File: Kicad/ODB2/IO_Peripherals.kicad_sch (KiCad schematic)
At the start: 15 parts, among them J1 USB_B_Micro, U4 USBLC6-2P6

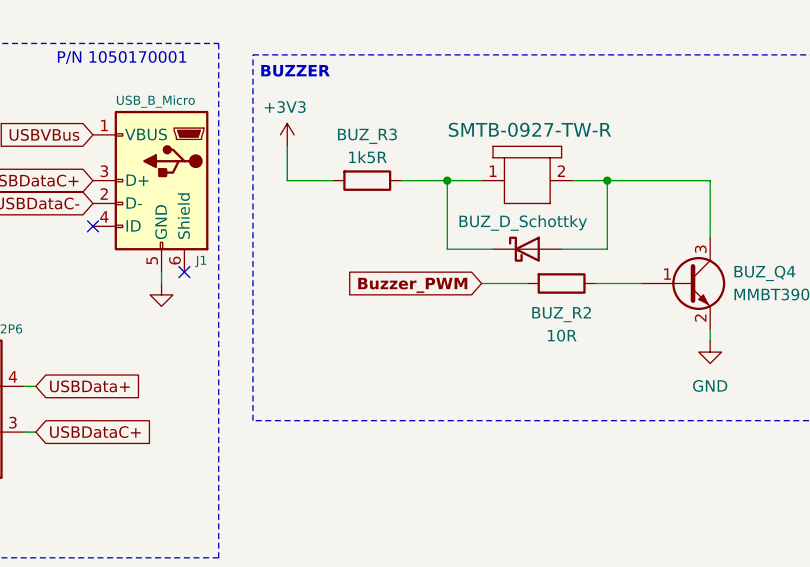
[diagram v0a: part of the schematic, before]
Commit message: merge all sensors to main page + fix NC
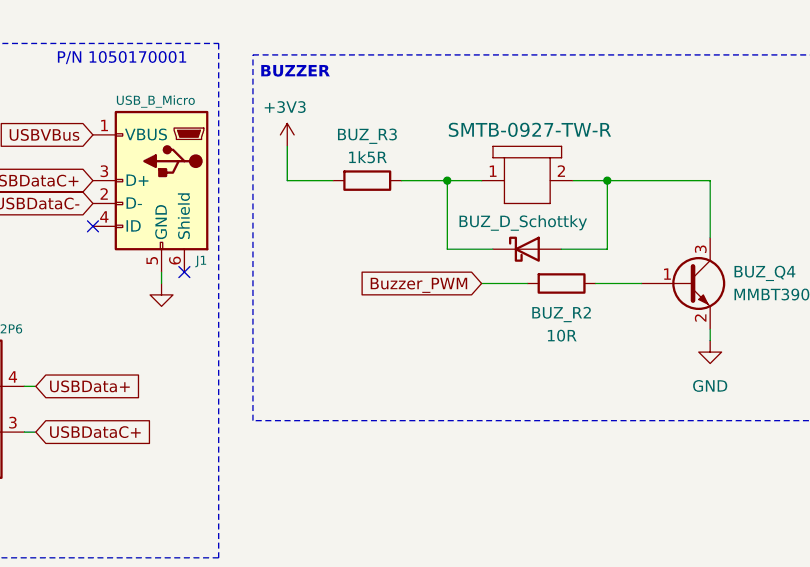
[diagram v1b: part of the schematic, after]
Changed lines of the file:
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@@
 			(font
 				(size 1.27 1.27)
-				(thickness 0.254)
-				(bold yes)
+				(thickness 0.1588)
 			)
 			(justify right)
 		)
 		(property "Intersheetrefs" "${INTERSHEET_REFS}"
-			(at 119.6684 48.26 0)
+			(at 120.1444 48.26 0)
 			(effects
 				(font

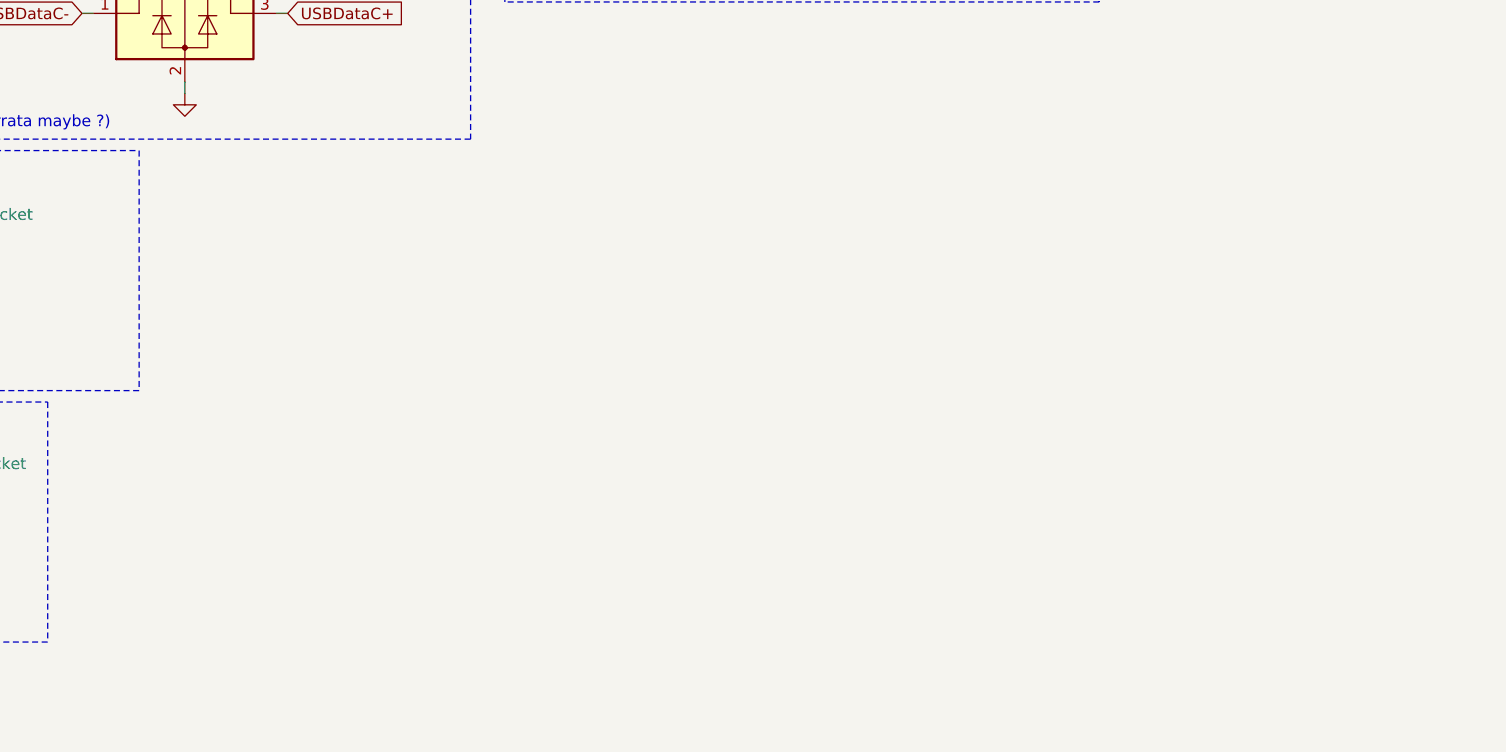
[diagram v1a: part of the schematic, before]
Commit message: delete hierarchie ODB
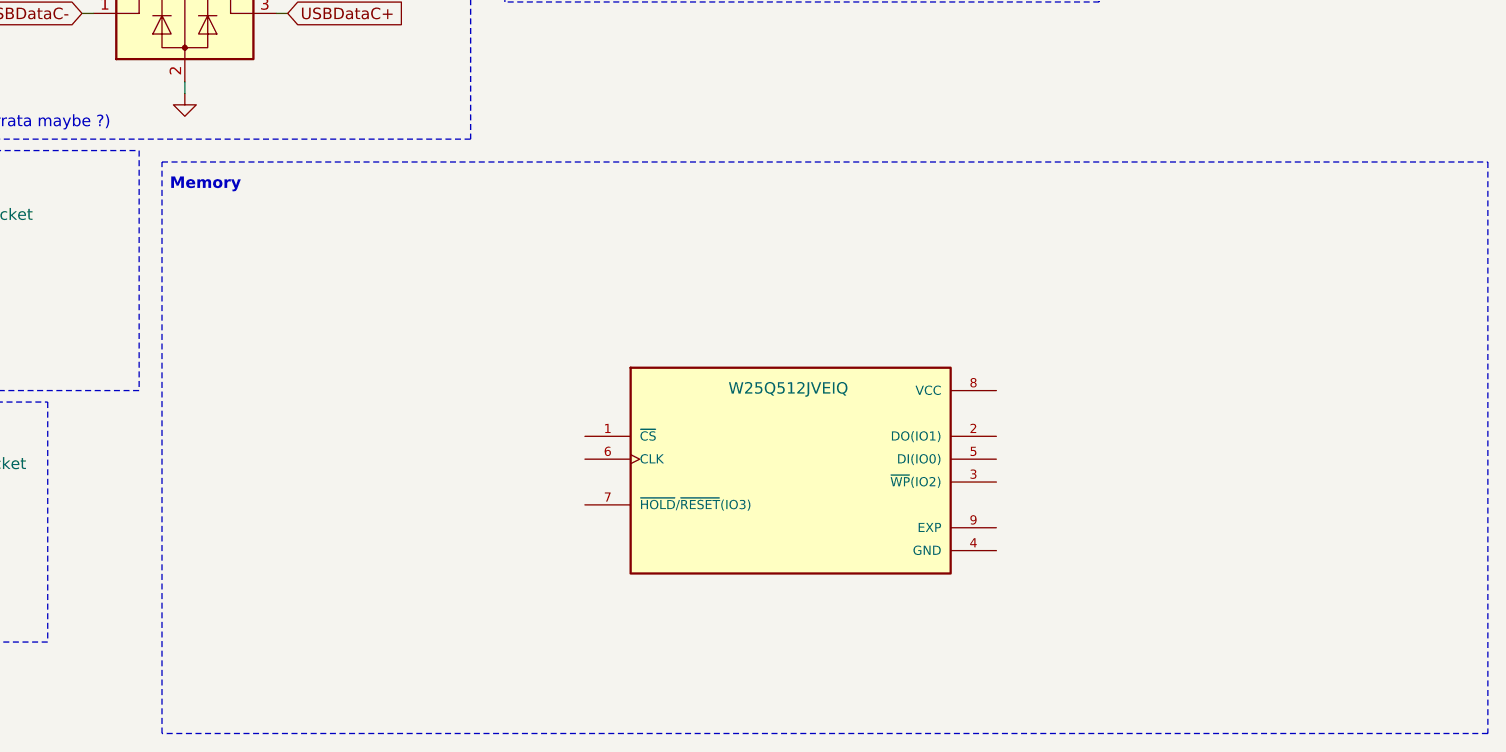
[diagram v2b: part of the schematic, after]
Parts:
- added U10: W25Q512JVEIQ, W25Q512JVEIQ:SON127P600X800X80-9N, symbol ODB_Lib:W25Q512JVEIQ
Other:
- note added: "Memory"
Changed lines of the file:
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@@
+	)
+	(rectangle
+		(start 71.12 81.28)
+		(end 218.44 144.78)
+		(stroke
+			(width 0)
+			(type dash)
+		)
+		(fill
+			(type none)
+		)
 	)
 	(rectangle
@@
 		)
 	)
+	(text "Memory"
+		(exclude_from_sim no)
+		(at 75.946 83.82 0)
+		(effects
+			(font
+				(size 1.27 1.27)
+				(thickness 0.254)
+				(bold yes)
+			)
+		)
+	)
 	(text "MICRO USB"
 		(exclude_from_sim no)
@@
 					(unit 1)
 				)
+			)
+		)
+	)
+	(symbol
+		(lib_id "ODB_Lib:W25Q512JVEIQ")
+		(at 140.97 116.84 0)
+		(unit 1)
+		(exclude_from_sim no)
+		(in_bom yes)
+		(on_board yes)
+		(dnp no)
+		(property "Reference" "U10"
+			(at 140.97 99.06 0)
+			(effects
+				(font
+					(size 1.27 1.27)
+				)
+				(hide yes)
+			)
+		)
+		(property "Value" "W25Q512JVEIQ"
+			(at 140.716 106.426 0)
+			(effects
+				(font
+					(size 1.27 1.27)
+				)
+			)
+		)
+		(property "Footprint" "W25Q512JVEIQ:SON127P600X800X80-9N"
+			(at 151.384 137.922 0)
+			(effects
+				(font
+					(size 1.27 1.27)
+				)
+				(justify bottom)
+				(hide yes)
+			)
+		)
+		(property "Datasheet" ""
+			(at 140.97 116.84 0)
+			(effects
+				(font
+					(size 1.27 1.27)
+				)
+				(hide yes)
+			)
+		)
+		(property "Description" ""
+			(at 140.97 116.84 0)
+			(effects
+				(font
+					(size 1.27 1.27)
+				)
+				(hide yes)
+			)
+		)
+		(property "PARTREV" "G"
+			(at 137.414 131.572 0)
+			(effects
+				(font
+					(size 1.27 1.27)
+				)
+				(justify bottom)
+				(hide yes)
+			)
+		)
+		(property "SNAPEDA_PN" "W25Q512JVEIQ"
+			(at 147.32 131.318 0)
+			(effects
+				(font
+					(size 1.27 1.27)
+				)
+				(justify bottom)
+				(hide yes)
+			)
+		)
+		(property "MANUFACTURER" "Winbond Electronics"
+			(at 148.59 133.096 0)
+			(effects
+				(font
+					(size 1.27 1.27)
+				)
+				(justify bottom)
+				(hide yes)
+			)
+		)
+		(property "MAXIMUM_PACKAGE_HEIGHT" "0.8 mm"
+			(at 137.668 134.874 0)
+			(effects
+				(font
+					(size 1.27 1.27)
+				)
+				(justify bottom)
+				(hide yes)
+			)
+		)
+		(property "STANDARD" "IPC 7351B"
+			(at 147.574 135.128 0)
+			(effects
+				(font
+					(size 1.27 1.27)
+				)
+				(justify bottom)
+				(hide yes)
+			)
+		)
+		(pin "9"
+		)
+		(pin "1"
+		)
+		(pin "5"
+		)
+		(pin "6"
+		)
+		(pin "8"
+		)
+		(pin "4"
+		)
+		(pin "3"
+		)
+		(pin "7"
+		)
+		(pin "2"
+		)
+		(instances
+			(project ""
+				(path "/4b06c5d1-aa8b-48ed-8972-b43a60cfab78/93865dc8-71fa-4dc6-90ce-f5a9779dfd41"
+					(reference "U10")
+					(unit 1)
+				)

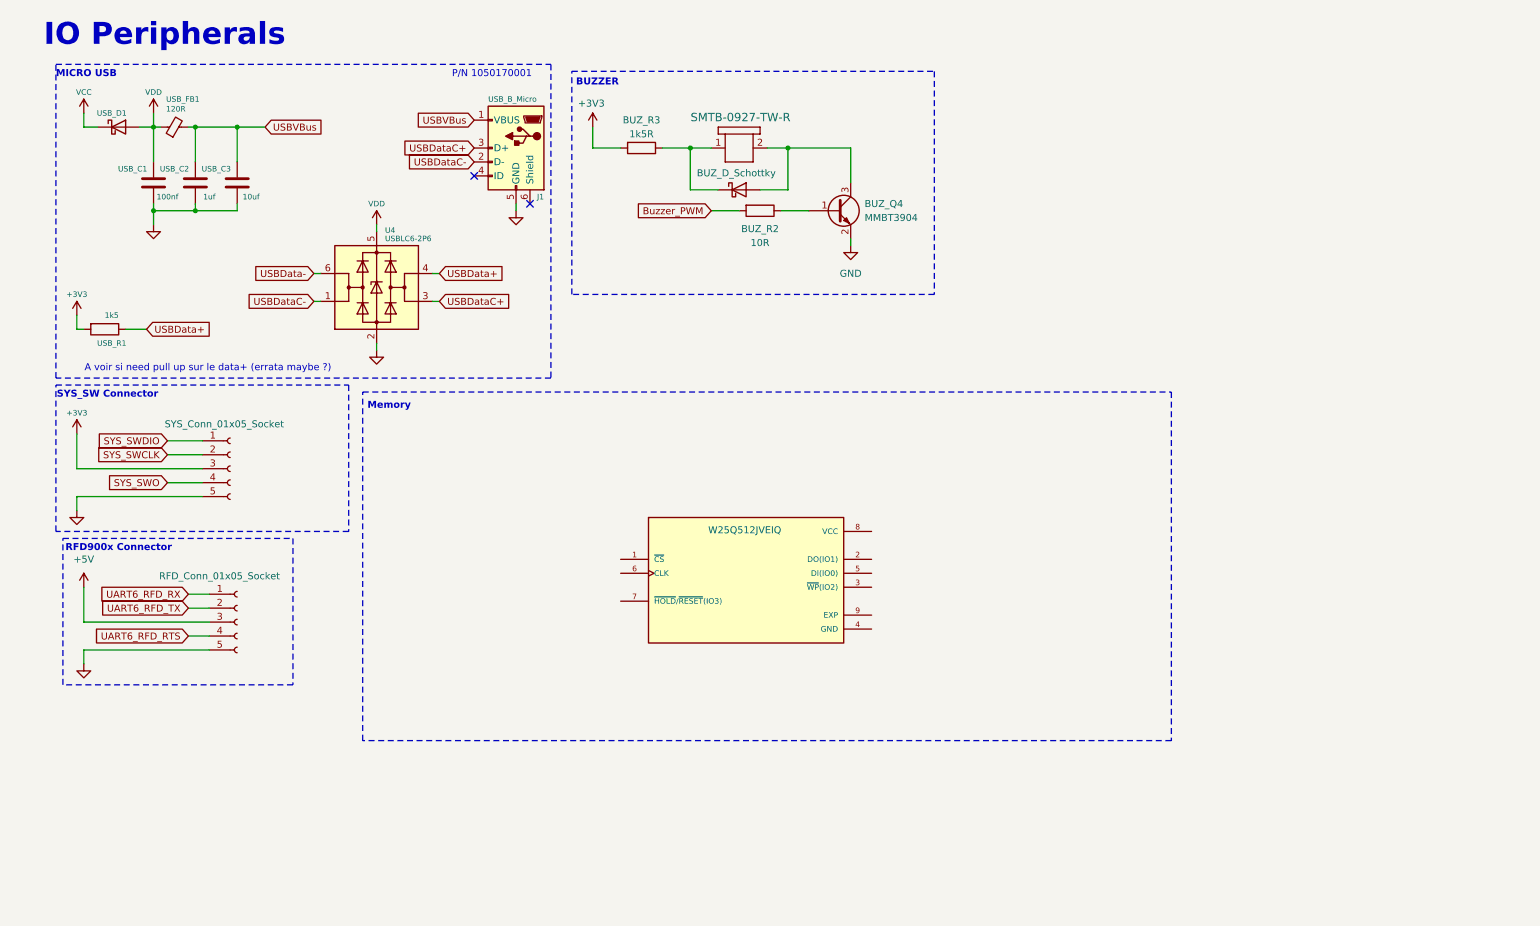
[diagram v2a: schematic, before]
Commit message: add W25Q512JV
vérifier pinout communication
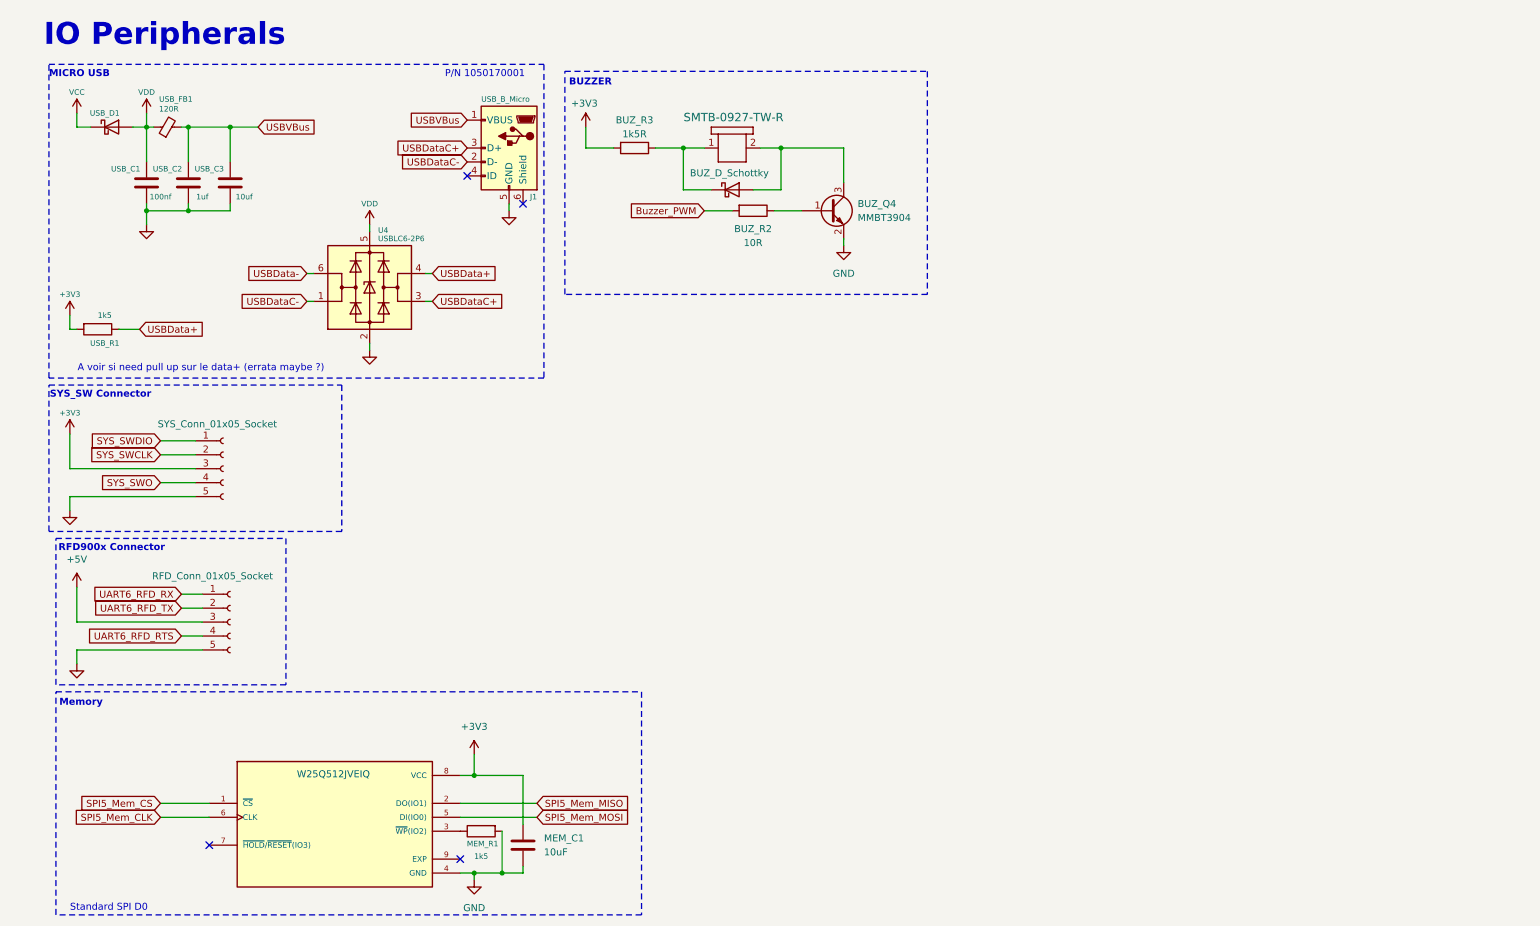
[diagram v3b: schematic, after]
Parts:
- added MEM_C1: 10uF, symbol Device:C
- added MEM_R1: 1k5, Resistor_SMD:R_0805_2012Metric, symbol Device:R
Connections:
- net +3V3: now also U10.8 (VCC), MEM_C1.2
- net GND: now also U10.4 (GND), MEM_C1.1, MEM_R1.2
- net SPI5_Mem_CS: now reaches U10.1 (~{CS})
- net SPI5_Mem_MISO: now reaches U10.2 (DO(IO1))
- net at U10.3 (~{WP}(IO2)): now also MEM_R1.1
- net SPI5_Mem_MOSI: now reaches U10.5 (DI(IO0))
- net SPI5_Mem_CLK: now reaches U10.6 (CLK)
- no-connect marks 2 -> 4
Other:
- note added: "Standard SPI D0"
- moved on the sheet: BUZ_Q4, BUZ_R2, BUZ_R3, J1, U4, USB_C1, USB_C2, USB_C3, USB_D1, USB_FB1, USB_R1

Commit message: fix circuit
reste à verifier les pinout
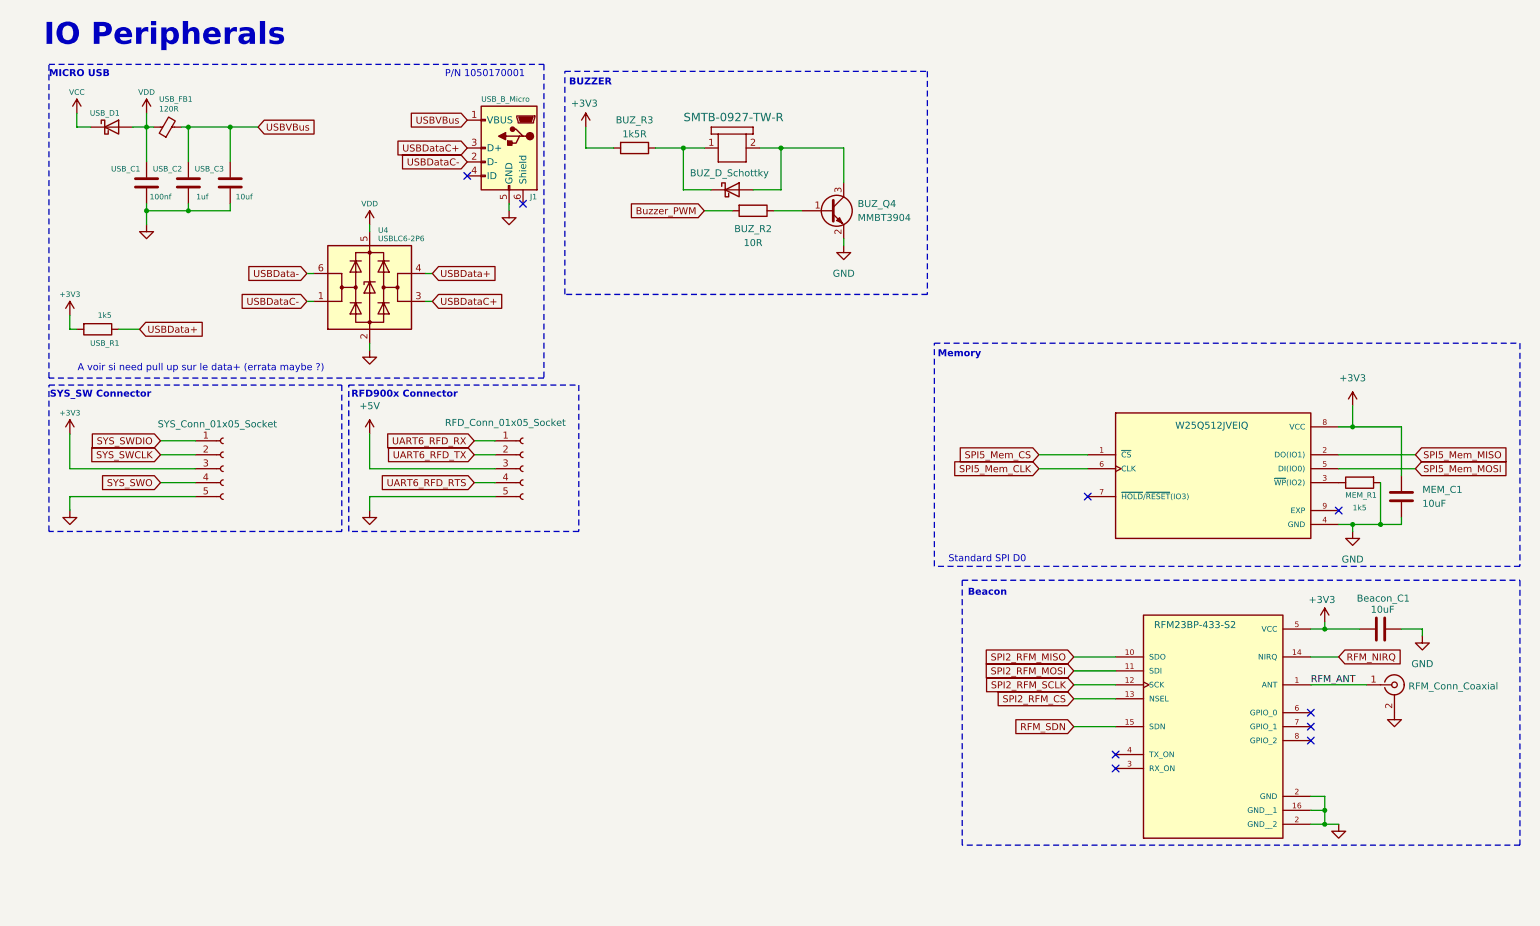
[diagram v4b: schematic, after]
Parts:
- added Beacon_C1: 10uF, symbol Device:C
- added J5: RFM_Conn_Coaxial, symbol Connector:Conn_Coaxial
- added U9: RFM23BP-433-S2, ODB:RFM22B-433-S2, symbol ODB2:RFM23BP-433-S2
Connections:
- net +3V3: now also Beacon_C1.1, U9.5 (VCC)
- net GND: now also Beacon_C1.2, J5.2 (Ext), U9.16 (GND__1), U9.2 (GND__2)
- new net RFM_ANT: J5.1 (In), U9.1 (ANT)
- new net RFM_NIRQ: U9.14 (NIRQ)
- new net RFM_SDN: U9.15 (SDN)
- new net SPI2_RFM_CS: U9.13 (NSEL)
- new net SPI2_RFM_MISO: U9.10 (SDO)
- new net SPI2_RFM_MOSI: U9.11 (SDI)
- new net SPI2_RFM_SCLK: U9.12 (SCK)
- no-connect marks 4 -> 9
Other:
- note added: "Beacon"
- moved on the sheet: MEM_C1, MEM_R1

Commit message: edit 2e iteration
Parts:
- added IO_LED1: Red, symbol Device:LED
- added LED_R1: 1k5, symbol Device:R
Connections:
- net GND: now also IO_LED1.1 (K)
- new net: IO_LED1.2 (A), LED_R1.1
- new net IO_RLED: LED_R1.2
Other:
- note added: "CRITICAL RED LIGHT"
